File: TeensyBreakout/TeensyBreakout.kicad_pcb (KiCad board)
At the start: 2 copper layers, 85.5 x 77.4 mm, 23 parts, among them J1 EncDriveRight, J10 MC3, J11 CurrSB, J12 UWB, J13 UVB Divider, J14 3.3V, J15 Relay, J2 EncDriveLeft, J3 EncExcavation, J4 Load Cell 1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

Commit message: minor changes
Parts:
- moved R2 3.50 mm to (188.8, 103.5)
- moved R1 1.14 mm to (203.2, 69.7)
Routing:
- net +3.3V: track 97.7 -> 6.61 mm
- net GND: track 25.4 -> 16.2 mm, vias 4 -> 3
- net /RX: track 57.1 -> 54.1 mm
- net /WCLK2: track 11.6 -> 10.8 mm
- added copper zone on B.Cu, net +3.3V

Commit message: Changes
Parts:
- removed J14: 3.3V, teensy:2pinJST
- removed J6: GND, teensy:5pinJST
- removed J7: 5V, teensy:3pinJST
- J4: value Load Cell 1 -> Load Cell 2; footprint teensy:2pinJST -> teensy:4pinJST
- J5: value Load Cell 2 -> Load Cell 1; footprint teensy:2pinJST -> teensy:4pinJST
- moved J5 20.3 mm to (152.0, 94.0)
- moved J15 9.99 mm to (152.0, 84.0)
- moved J4 4.34 mm to (152.0, 108.5)
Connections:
- J1 pad 2: unconnected-(J1-Pin_2-Pad2) -> +5V
- J1 pad 4: unconnected-(J1-Pin_4-Pad4) -> GND
- J2 pad 2: unconnected-(J2-Pin_2-Pad2) -> +5V
- J2 pad 4: unconnected-(J2-Pin_4-Pad4) -> GND
- J3 pad 2: unconnected-(J3-Pin_2-Pad2) -> +5V
- J3 pad 4: unconnected-(J3-Pin_4-Pad4) -> GND
- J4 pad 1: /WCLK1 -> /WCLK2
- J4 pad 2: /WDAT1 -> /WDAT2
- J5 pad 1: /WCLK2 -> /WCLK1
- J5 pad 2: /WDAT2 -> /WDAT1
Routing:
- net +5V: track 140.9 -> 160.0 mm
- net /Relay: track 40.0 -> 44.6 mm
- net /WDAT1: track 8.67 -> 11.2 mm
- net /WCLK1: track 8.69 -> 11.2 mm
- net +3.3V: track 6.61 -> 4.15 mm
- net /WCLK2: track 10.8 -> 8.77 mm
- net /WDAT2: track 10.8 -> 8.76 mm

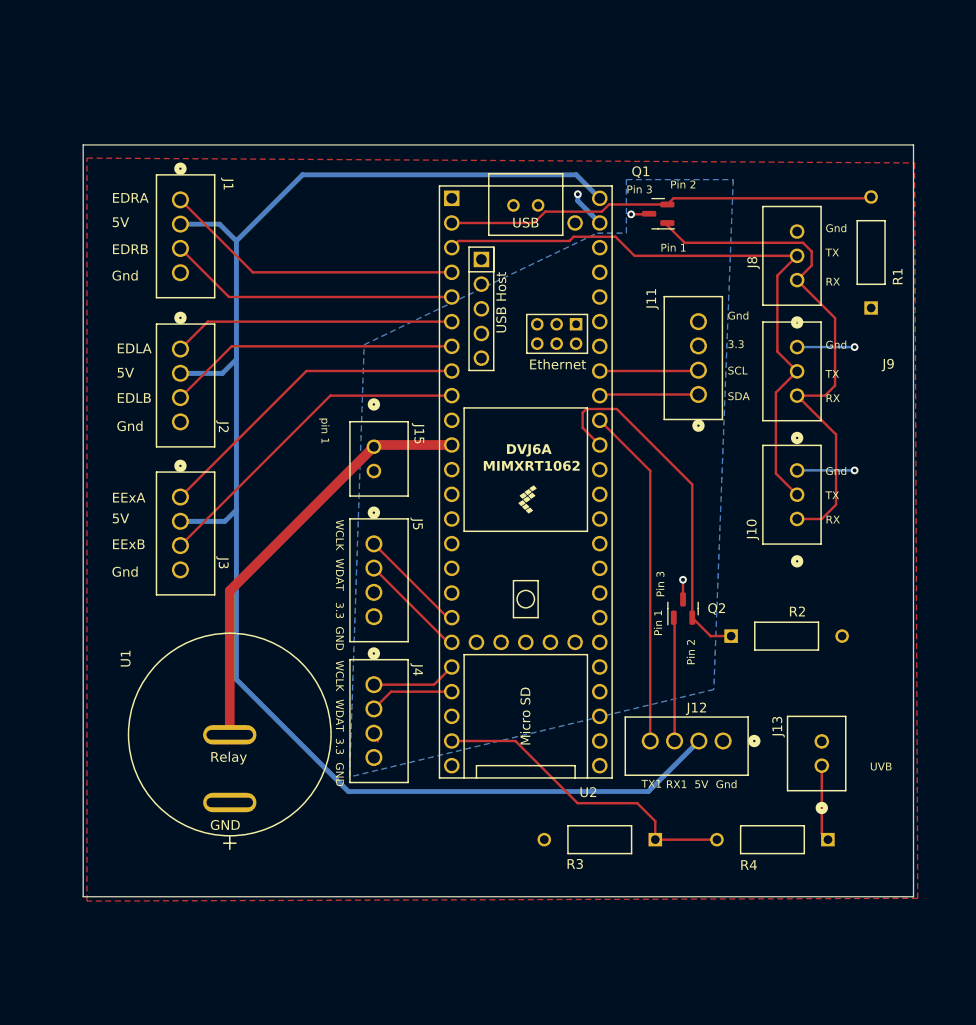
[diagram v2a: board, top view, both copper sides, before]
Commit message: added silkscreen
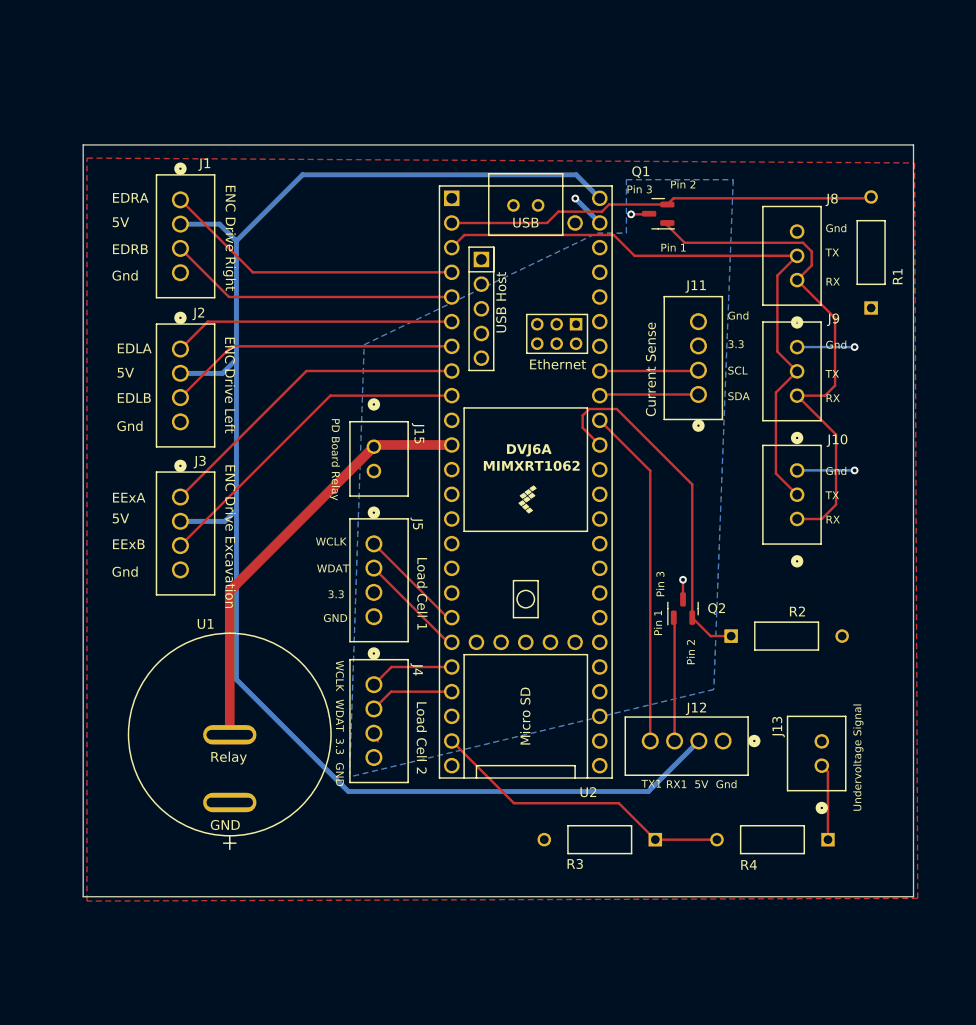
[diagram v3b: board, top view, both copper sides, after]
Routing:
- net /UnderVolt: track 32.6 -> 31.5 mm
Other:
- board text added: "Current Sense"
- board text added: "ENC Drive Excavation"
- board text added: "ENC Drive Left"
- board text added: "ENC Drive Right"
- board text added: "Load Cell 1"
- board text added: "Load Cell 2"
- board text added: "PD Board Relay"
- board text added: "Undervoltage Signal"
- board text removed: "UVB"
- board text removed: "pin 1"

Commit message: added mounting
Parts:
- added ?: , , F.Cu at (124.3, 134.1)
- added ?: , , F.Cu at (202.9, 134.1)
- added ?: , , F.Cu at (203.0, 49.5)
- added ?: , , F.Cu at (124.3, 49.5)
- added REF**: MountingHole_3.7mm_Pad, MountingHole:MountingHole_3.7mm_Pad, F.Cu at (124.3, 49.5)
- added REF**: MountingHole_3.7mm_Pad, MountingHole:MountingHole_3.7mm_Pad, F.Cu at (202.9, 134.1)
- added REF**: MountingHole_3.7mm_Pad, MountingHole:MountingHole_3.7mm_Pad, F.Cu at (203.0, 49.5)
- added REF**: MountingHole_3.7mm_Pad, MountingHole:MountingHole_3.7mm_Pad, F.Cu at (124.3, 134.1)
- moved J1 7.55 mm to (139.5, 60.0)
- moved J2 7.55 mm to (139.5, 75.4)
- moved J3 7.55 mm to (139.5, 90.6)
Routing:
- net /EDRA: track 31.0 -> 23.0 mm
- net /EDRB: track 30.0 -> 22.0 mm
- net /EExA: track 33.3 -> 26.5 mm
- net /EDLA: track 29.1 -> 22.3 mm
- net /EDLB: track 30.1 -> 23.3 mm
- net /EExB: track 34.3 -> 28.7 mm
- net +5V: track 160.0 -> 163.2 mm
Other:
- board size 85.5 x 77.4 mm -> 90.8 x 95.4 mm

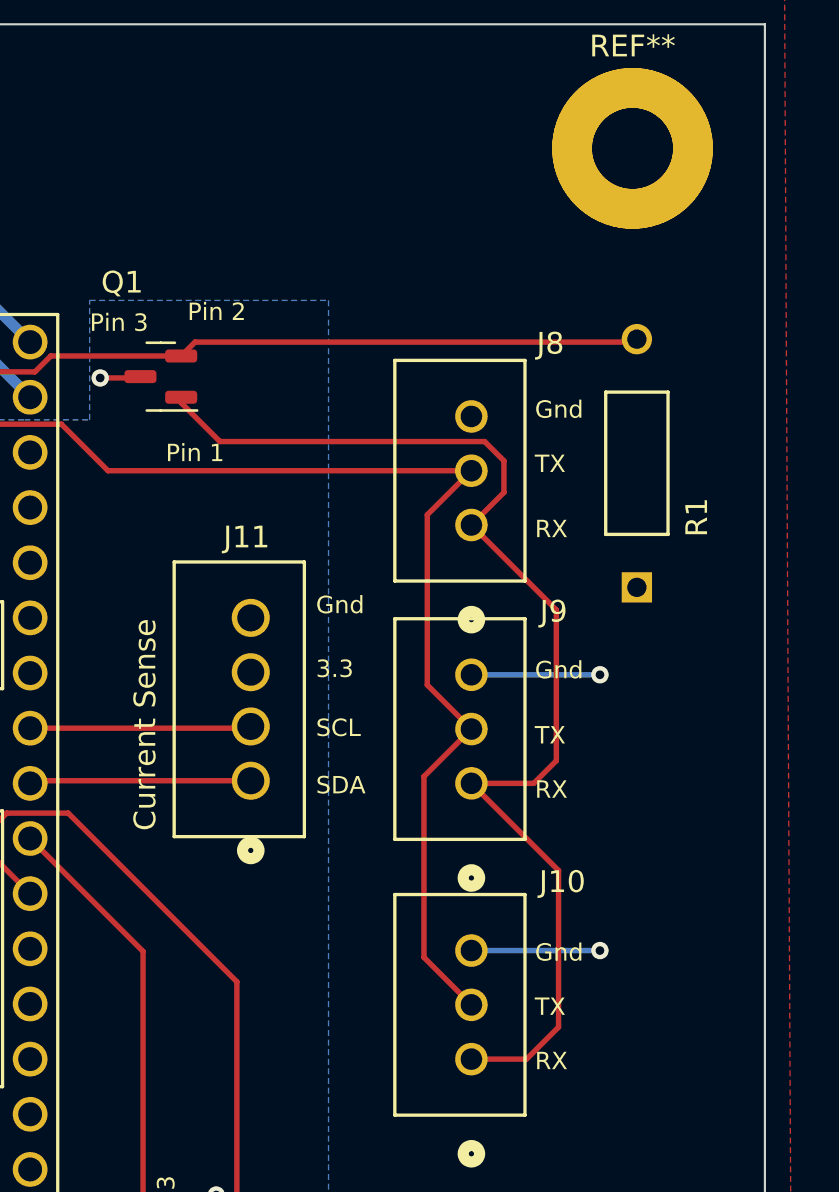
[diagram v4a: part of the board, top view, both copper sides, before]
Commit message: added fuses to gnd input from MCs
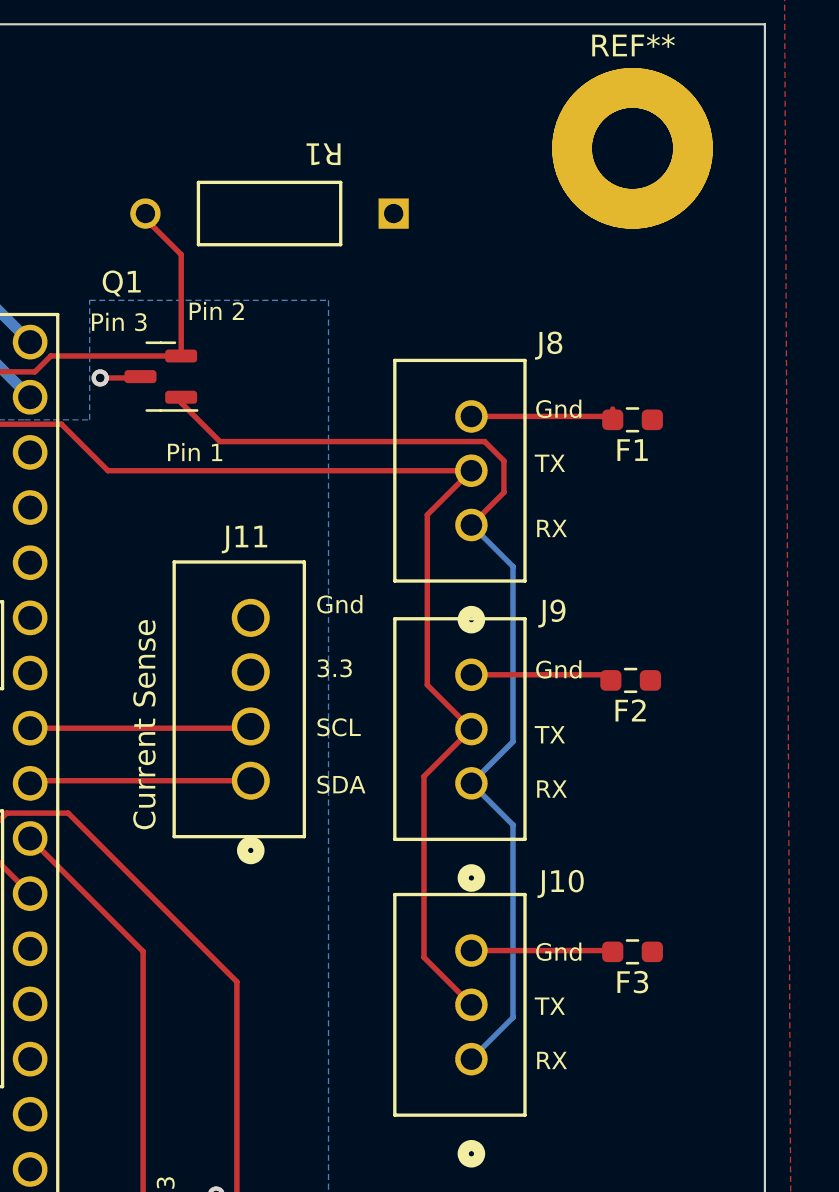
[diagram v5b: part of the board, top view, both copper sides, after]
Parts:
- added F1: Fuse, Resistor_SMD:R_0603_1608Metric_Pad0.98x0.95mm_HandSolder, F.Cu at (203.0, 62.0)
- added F2: Fuse, Resistor_SMD:R_0603_1608Metric_Pad0.98x0.95mm_HandSolder, F.Cu at (202.9, 74.0)
- added F3: Fuse, Resistor_SMD:R_0603_1608Metric_Pad0.98x0.95mm_HandSolder, F.Cu at (203.0, 86.5)
- moved R1 20.5 mm to (192.0, 52.5), turned to 180 degrees
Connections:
- J10 pad 3: GND -> /MGND3
- J8 pad 3: GND -> /MGND1
- J9 pad 3: GND -> /MGND2
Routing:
- net Net-(Q1-S): track 44.3 -> 30.2 mm
- net GND: track 15.9 -> 3.56 mm, vias 3 -> 1
- net /MGND1: track 0.00 -> 7.29 mm
- net /RX: track 54.1 -> 47.6 mm
- net /MGND3: track 0.00 -> 6.53 mm
- net /MGND2: track 0.00 -> 6.53 mm

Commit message: minor changes
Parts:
- removed ? (x4): , 
- removed F2, F3: Fuse, Resistor_SMD:R_0603_1608Metric_Pad0.98x0.95mm_HandSolder
- added MC_5V_IN: TestPoint, Connector_Pin:Pin_D0.9mm_L10.0mm_W2.4mm_FlatFork, F.Cu at (195.0, 56.0)
- added R5: 0, Resistor_SMD:R_0805_2012Metric_Pad1.20x1.40mm_HandSolder, F.Cu at (175.0, 52.5)
- moved R1 7.95 mm to (186.0, 47.3), turned to -90 degrees
- moved U1 4.86 mm to (133.5, 123.8)
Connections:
- F1 pad 2: /MGND1 -> /MGND
- J10 pad 3: /MGND3 -> /MGND
- J8 pad 3: /MGND1 -> /MGND
- J9 pad 3: /MGND2 -> /MGND
- U2 pad 48: +5V -> /5V_Teensy
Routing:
- net /MGND: track 0.00 -> 36.6 mm
- net +5V: track 163.2 -> 185.6 mm, vias 0 -> 1
- net /MGND1: track 7.29 -> 0.00 mm
- net /MGND3: track 6.53 -> 0.00 mm
- net /MGND2: track 6.53 -> 0.00 mm
- net /5V_Teensy: track 0.00 -> 5.03 mm
- net /Relay: track 44.6 -> 48.6 mm
- net Net-(Q1-S): track 30.2 -> 26.9 mm
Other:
- board text added: "NC"
- board text added: "PD Board"
- board text added: "Signal"
- board text added: "UWB"
- board text added: "Undervoltage"
- board text removed: "PD Board Relay"
- board text removed: "Pin 1"
- board text removed: "Pin 2"
- board text removed: "Pin 3"
- board text removed: "Undervoltage Signal"
